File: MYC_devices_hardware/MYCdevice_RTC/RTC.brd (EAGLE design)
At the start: 64.1 x 54 mm, 30 parts, among them IC1 MEGA8-P, IC2 7805T, Q1 20MHz, X1 8-15V, X2 1503_09, X3 1503_09

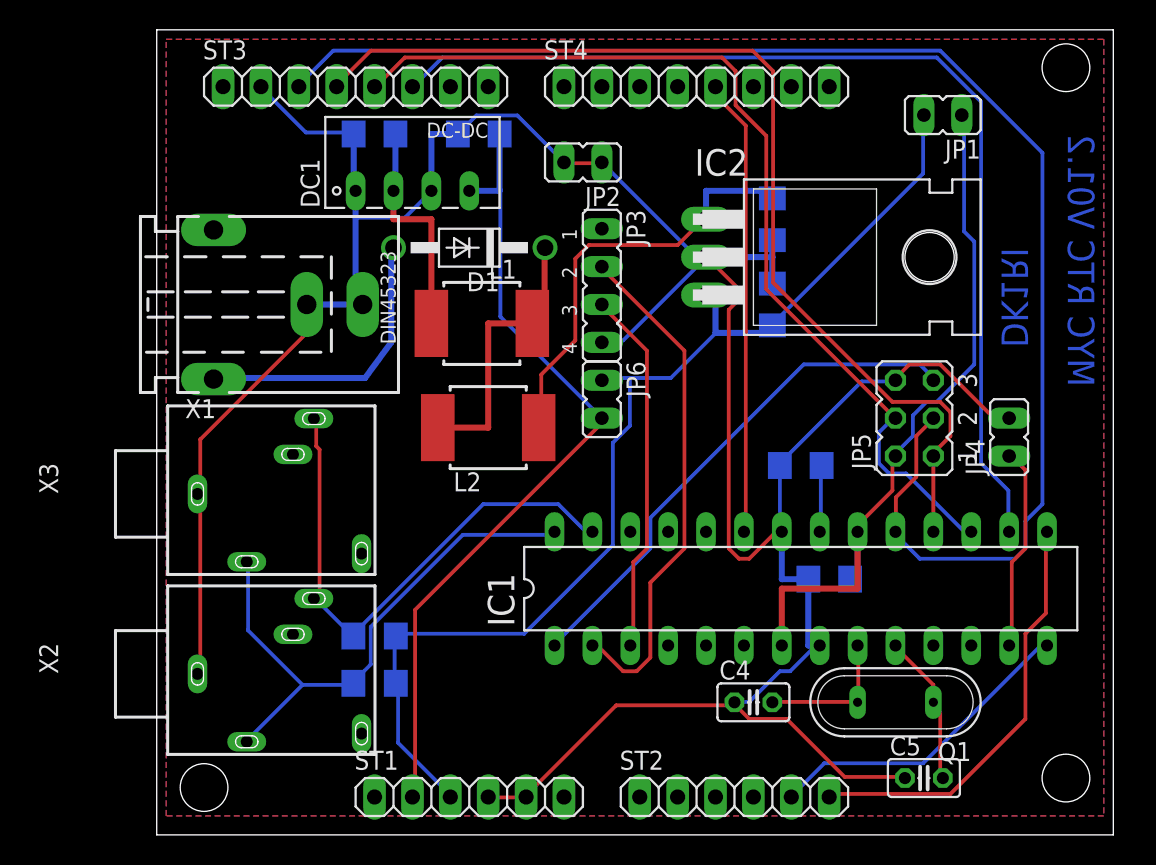
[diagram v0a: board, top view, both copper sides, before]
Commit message: board with RS232, bascom with includes
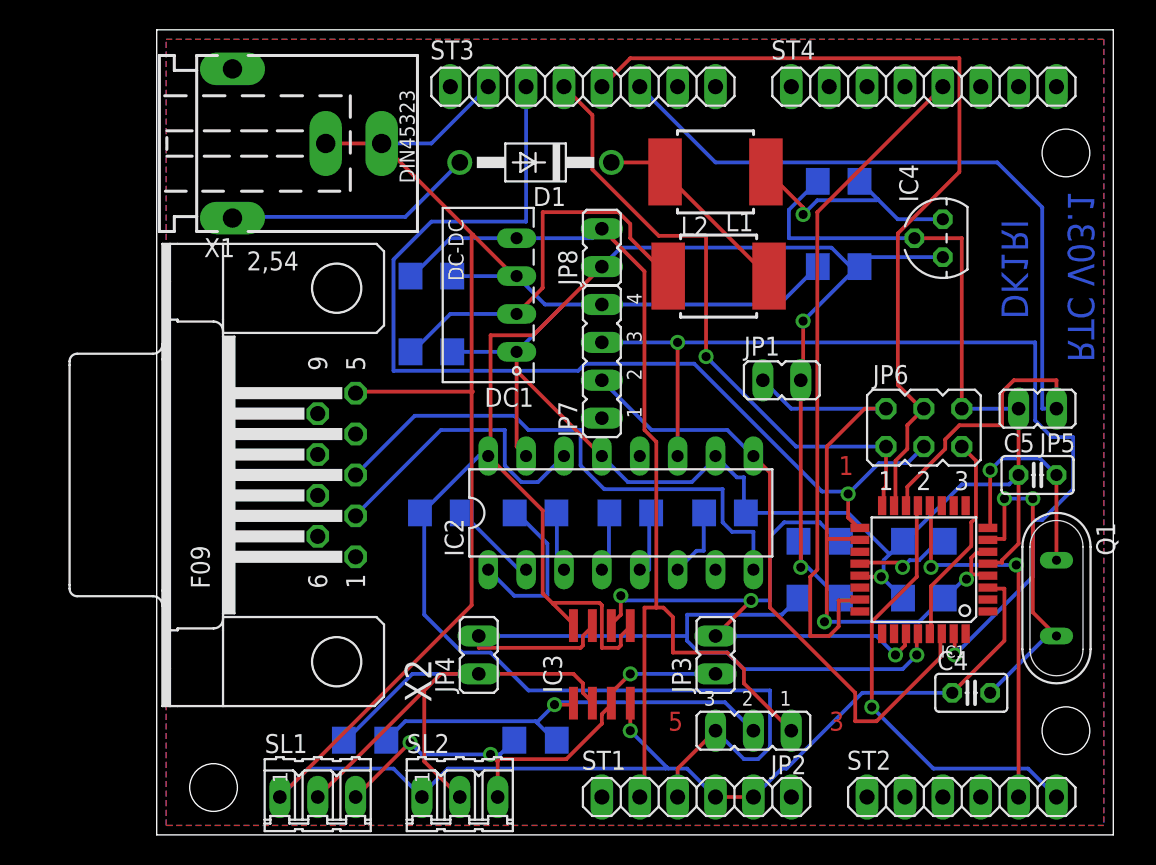
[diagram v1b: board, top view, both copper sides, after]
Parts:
- removed X3: 1503_09, con-lumberg:1503_09
- added C10, C11, C12, C9: 22uF, rcl:C1206
- added IC3: PCA9517, PCA9517:SO-08
- added IC4: 78L08Z, linear:TO92
- added JP7: USB, jumper:JP4
- added JP8: USB2, jumper:JP1
- added R1, R2: see manual, resistor:R1206
- added SL1, SL2: I2C, con-amp-quick:03P
- C1, C2, C3, C6, C7, C8: value 22uF 1210 -> 22uF
- IC1: value MEGA8-P -> MEGA8-AI; device atmel:DIL28-3 -> atmel:TQFP32-08
- IC2: value 7805T -> MAX232; device linear:TO220H -> maxim:DIL16
- JP2: value GND -> 3V/5V; device jumper:JP1 -> jumper:JP2
- JP3: value USB -> SDA; device jumper:JP4 -> jumper:JP1
- JP4: value Reset -> SCL
- JP5: value ISP -> Reset; device jumper:JP3Q -> jumper:JP1
- JP6: value USB2 -> ISP; device jumper:JP1 -> jumper:JP3Q
- R3, R4: value 4k7 -> see manual
- X2: value 1503_09 -> RS232; device con-lumberg:1503_09 -> con-subd:F09H
- moved JP2 39.8 mm to (39.4, 6.99), turned to 180 degrees
- moved JP4 38.4 mm to (21.0, 12.1)
- moved R3 30.5 mm to (43.8, 19.7), turned to 180 degrees
- moved R4 30.4 mm to (43.8, 15.9)
- moved C7 27.4 mm to (31.1, 21.6), turned to 180 degrees
- moved JP3 25.9 mm to (36.8, 12.1), turned to 0 degrees
- moved C8 25.8 mm to (18.4, 21.6), turned to 180 degrees
- moved IC2 23.4 mm to (30.5, 21.6), turned to 0 degrees
- moved L2 22.9 mm to (36.8, 44.5)
- moved C5 21.7 mm to (58.4, 24.1)
- moved JP6 21.7 mm to (50.8, 27.3), turned to 0 degrees
- moved JP1 20.8 mm to (41.3, 30.5), turned to 270 degrees
- moved C6 20.2 mm to (24.8, 21.6), turned to 180 degrees
- moved X2 17.6 mm to (11.4, 24.1)
- moved L1 16.2 mm to (37.0, 37.5)
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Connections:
- new net N$11: IC3.2, JP4.1, R2.2, SL1.2, SL2.2
- new net N$12: IC3.3, JP3.1, R1.2, SL1.3, SL2.3
- new net N$13: IC2.14, X2.2
- new net N$14: C8.2, IC2.2
- new net N$16: C9.1, IC2.6
- new net N$21: IC3.1, JP2.2, R1.1, R2.1
- new net N$23: C6.1, IC2.1
- new net N$24: C6.2, IC2.3
- new net N$25: C7.1, IC2.4
- new net N$26: C7.2, IC2.5
- net GND: now also C10.2, C11.2, C12.2, C9.2, IC1.21, IC1.3, IC1.5, IC2.10, IC2.13, IC2.15, IC3.4, IC4.2, JP5.2, JP6.6, JP7.4, SL1.1, SL2.1, X2.5; no longer C6.2, C7.2, C8.2, IC1.22, IC1.8, IC2.2, JP2.1, JP2.2, JP3.4, JP4.2, JP5.6, X2.1, X3.1
- net N$10: now also IC1.13; no longer IC1.15
- net N$15: now also IC1.16, JP6.1; no longer IC1.18, JP5.1
- net N$18: now also IC1.29, JP6.5; no longer IC1.1, JP5.5
- net N$19: now also IC1.7; no longer IC1.9
- net N$2: now also IC1.12; no longer IC1.14
- net N$20: now also IC1.17, JP6.3; no longer IC1.19, JP5.3
- net N$22: now also IC3.7, JP4.2; no longer X2.2, X3.2
- net N$28: now also IC1.15, JP6.4; no longer IC1.17, JP5.4
- net N$3: now also C11.1; no longer C8.1
- net N$33: now also IC4.3; no longer IC2.1
- net N$35: now also IC1.20; no longer IC1.21
- net N$37: now also IC1.8; no longer IC1.10
- net N$4: now also IC1.14, JP5.1; no longer IC1.16
- net N$44: now also C10.1, IC1.18, IC1.4, IC1.6, JP6.2; no longer C6.1, IC1.20, IC1.7, JP5.2
- net N$5: now also IC3.6, JP3.2; no longer X2.3, X3.3
- net N$6: now also IC2.8, X2.3; no longer IC1.13, JP4.1
- net N$8: now also IC1.31, IC2.11, JP7.3; no longer IC1.3, JP3.3
- net N$9: now also IC1.30, IC2.9, JP7.2; no longer IC1.2, JP3.2
- net VDD: now also C8.1, IC2.16, IC3.5, IC3.8, IC4.1, JP2.3, JP8.1; no longer IC2.3, JP6.1
- net VSS: now also C12.1, JP2.1, JP8.2; no longer C7.1, JP6.2
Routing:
- net GND: track 200.9 -> 277.2 mm, vias 0 -> 2
- net VDD: track 75.9 -> 144.8 mm, vias 0 -> 2
- net N$11: track 0.00 -> 42.0 mm
- net N$8: track 24.6 -> 64.6 mm, vias 0 -> 2
- net N$12: track 0.00 -> 33.9 mm, vias 0 -> 3
- net N$21: track 0.00 -> 29.7 mm, vias 0 -> 1
- net N$20: track 99.3 -> 69.9 mm, vias 0 -> 1
- net N$15: track 69.1 -> 42.5 mm, vias 0 -> 1
- net N$6: track 13.7 -> 36.8 mm
- net N$18: track 35.0 -> 14.3 mm
- net N$13: track 0.00 -> 19.9 mm
- net N$1: track 30.8 -> 45.9 mm
- net N$33: track 30.7 -> 16.0 mm, vias 0 -> 1
- net VSS: track 54.7 -> 69.1 mm
- net N$22: track 37.8 -> 51.1 mm, vias 0 -> 1
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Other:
- board text added: "1"
- board text added: "3"
- board text added: "5"
- board text added: "RTC V03.1"
- board text removed: "MYC RTC V01.2"
